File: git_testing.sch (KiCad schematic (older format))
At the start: 1 part

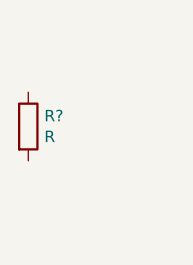
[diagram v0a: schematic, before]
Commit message: Added second resistor and power +3V3 / GND .
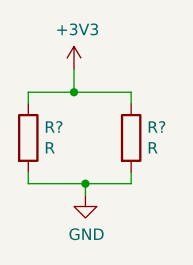
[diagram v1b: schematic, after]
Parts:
- added R?: R, symbol Device:R
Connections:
- net +3V3: now reaches R?.1
- net +3V3: now also R?.1
- net GND: now reaches R?.2
- net GND: now also R?.2
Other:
- moved on the sheet: R?
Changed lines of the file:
@@
 EESchema Schematic File Version 4
+LIBS:git_testing-cache
 EELAYER 30 0
 EELAYER END
@@
 L Device:R R?
 U 1 1 5E5BFE10
-P 5100 3750
-F 0 "R?" H 5170 3796 50  0000 L CNN
-F 1 "R" H 5170 3705 50  0000 L CNN
-F 2 "" V 5030 3750 50  0001 C CNN
-F 3 "~" H 5100 3750 50  0001 C CNN
-	1    5100 3750
+P 5100 3800
+F 0 "R?" H 5170 3846 50  0000 L CNN
+F 1 "R" H 5170 3755 50  0000 L CNN
+F 2 "" V 5030 3800 50  0001 C CNN
+F 3 "~" H 5100 3800 50  0001 C CNN
+	1    5100 3800
 	1    0    0    -1
 $EndComp
+$Comp
+L Device:R R?
+U 1 1 5E5BFF6D
+P 5550 3800
+F 0 "R?" H 5620 3846 50  0000 L CNN
+F 1 "R" H 5620 3755 50  0000 L CNN
+F 2 "" V 5480 3800 50  0001 C CNN
+F 3 "~" H 5550 3800 50  0001 C CNN
+	1    5550 3800
+	1    0    0    -1
+$EndComp
+Wire Wire Line
+	5100 3650 5100 3600
+Wire Wire Line
+	5100 3600 5300 3600
+Wire Wire Line
+	5550 3600 5550 3650
+Wire Wire Line
+	5100 3950 5100 4000
+Wire Wire Line
+	5100 4000 5350 4000
+Wire Wire Line
+	5550 4000 5550 3950
+$Comp
+L power:GND #PWR?
+U 1 1 5E5C04B6
+P 5350 4050
+F 0 "#PWR?" H 5350 3800 50  0001 C CNN
+F 1 "GND" H 5355 3877 50  0000 C CNN
+F 2 "" H 5350 4050 50  0001 C CNN
+F 3 "" H 5350 4050 50  0001 C CNN
+	1    5350 4050
+	1    0    0    -1
+$EndComp
+$Comp
+L power:+3V3 #PWR?
+U 1 1 5E5C085C
+P 5300 3500
+F 0 "#PWR?" H 5300 3350 50  0001 C CNN
+F 1 "+3V3" H 5315 3673 50  0000 C CNN
+F 2 "" H 5300 3500 50  0001 C CNN
+F 3 "" H 5300 3500 50  0001 C CNN
+	1    5300 3500
+	1    0    0    -1
+$EndComp
+Wire Wire Line
+	5300 3500 5300 3600
+Connection ~ 5300 3600
+Wire Wire Line
+	5300 3600 5550 3600
+Wire Wire Line
+	5350 4050 5350 4000
+Connection ~ 5350 4000
+Wire Wire Line
+	5350 4000 5550 4000
 $EndSCHEMATC
